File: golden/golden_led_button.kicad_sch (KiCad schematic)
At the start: 3 parts, among them SW1 SW_Push

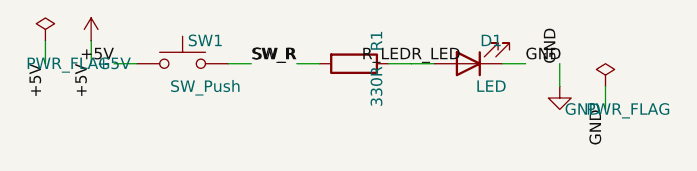
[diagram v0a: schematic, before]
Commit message: Fix pin transform via direct kicad-cli netlist probes; full pipeline green
The rotation direction (CW matrix in sheet axes) and mirror composition
(sheet-space, after rotation) cannot be derived from demo wire/pin triples
alone — symmetric parts at rot 90/270 give circular attributions, and the
initial CCW guess produced schematics that PASSED KiCad ERC with silently
crossed nets (R1 pins swapped). Caught by the §8.3-step-6 connectivity
round-trip, then settled by synthetic probe schematics fed to
kicad-cli sch export netlist for every rotation/mirror combination.

Adds: netlist generator + exported-netlist parser + partition comparison
(power symbols excluded, as KiCad does), end-to-end pipeline module,
ERC/symbols/netlist/pipeline test suites (44 tests).

Co-Authored-By: Claude Fable 5 <noreply@anthropic.com>
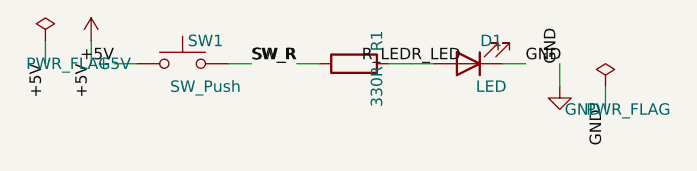
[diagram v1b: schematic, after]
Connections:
- net R_LED: now also R1.2; no longer R1.1
- net SW_R: now also R1.1; no longer R1.2
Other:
- moved on the sheet: R1
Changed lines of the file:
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@@
 	(symbol
 		(lib_id "Device:R")
-		(at 82.55 63.5 270)
+		(at 82.55 63.5 90)
 		(unit 1)
 		(body_style 1)
